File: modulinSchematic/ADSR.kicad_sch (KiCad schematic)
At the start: 0 parts

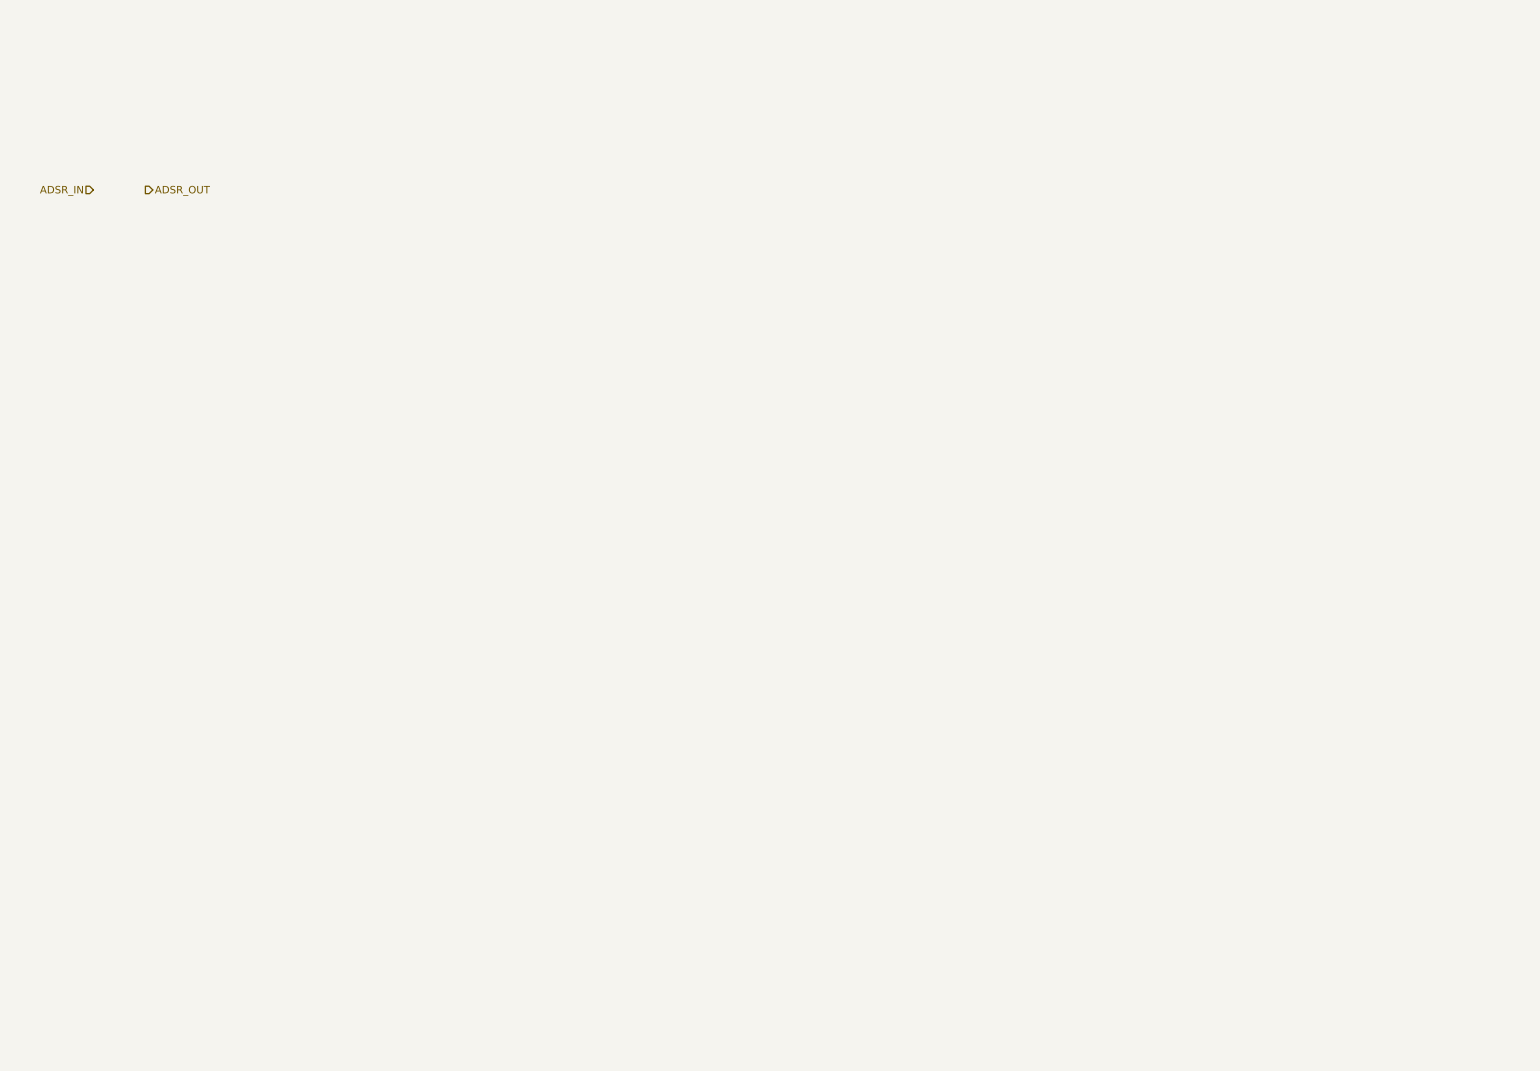
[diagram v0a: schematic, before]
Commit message: Add power schematic
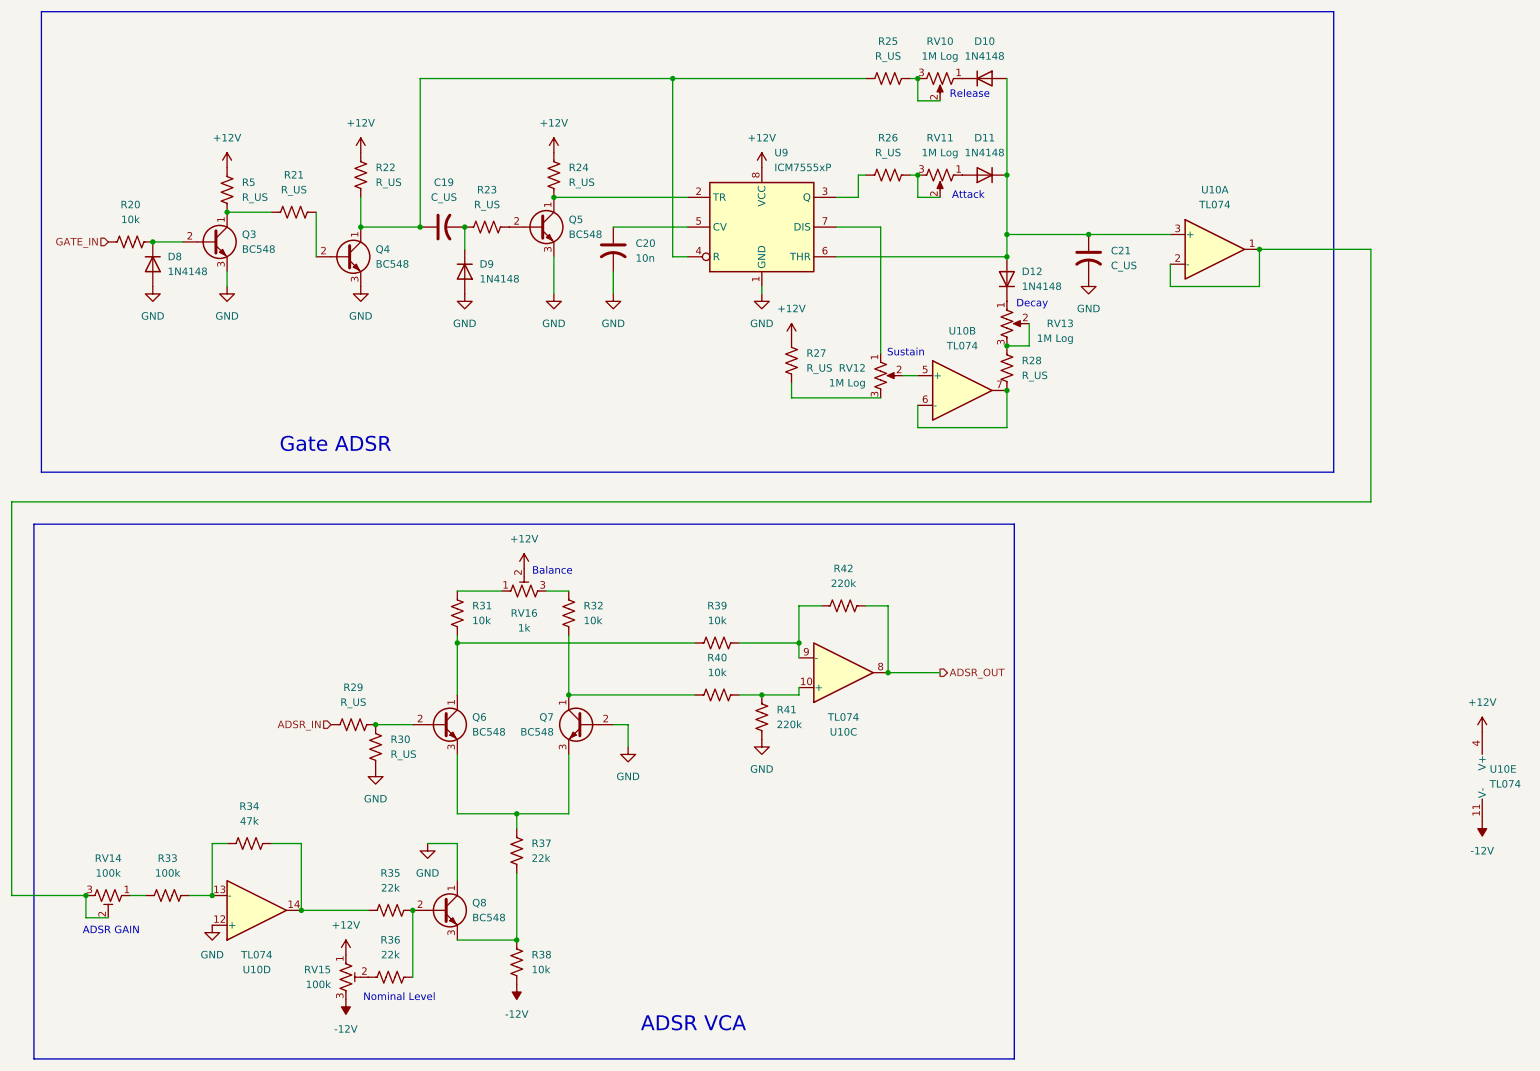
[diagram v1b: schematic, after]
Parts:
- added C19, C21: C_US, Capacitor_THT:CP_Radial_D4.0mm_P2.00mm, symbol Device:C_US
- added C20: 10n, Capacitor_THT:CP_Radial_D4.0mm_P2.00mm, symbol Device:C_US
- added D10, D11, D12, D8, D9: 1N4148, Diode_THT:D_DO-35_SOD27_P7.62mm_Horizontal, symbol Diode:1N4148
- added Q3, Q4, Q5, Q6, Q7, Q8: BC548, Package_TO_SOT_THT:TO-92_Inline, symbol Transistor_BJT:BC548
- added R20, R31, R32, R38, R39, R40: 10k, Resistor_THT:R_Axial_DIN0207_L6.3mm_D2.5mm_P10.16mm_Horizontal, symbol Device:R_US
- added R21, R22, R23, R24, R25, R26, R27, R28, R29, R30, R5: R_US, Resistor_THT:R_Axial_DIN0207_L6.3mm_D2.5mm_P10.16mm_Horizontal, symbol Device:R_US
- added R33: 100k, Resistor_THT:R_Axial_DIN0207_L6.3mm_D2.5mm_P10.16mm_Horizontal, symbol Device:R_US
- added R34: 47k, Resistor_THT:R_Axial_DIN0207_L6.3mm_D2.5mm_P10.16mm_Horizontal, symbol Device:R_US
- added R35, R36, R37: 22k, Resistor_THT:R_Axial_DIN0207_L6.3mm_D2.5mm_P10.16mm_Horizontal, symbol Device:R_US
- added R41, R42: 220k, Resistor_THT:R_Axial_DIN0207_L6.3mm_D2.5mm_P10.16mm_Horizontal, symbol Device:R_US
- added RV10, RV11, RV12, RV13: 1M Log, TerminalBlock:TerminalBlock_MaiXu_MX126-5.0-03P_1x03_P5.00mm, symbol Device:R_Potentiometer_US
- added RV14, RV15: 100k, Potentiometer_THT:Potentiometer_Bourns_3266Y_Vertical, symbol Device:R_Potentiometer_Trim_US
- added RV16: 1k, Potentiometer_THT:Potentiometer_Bourns_3266Y_Vertical, symbol Device:R_Potentiometer_Trim_US
- added U10: TL074, Package_DIP:DIP-14_W7.62mm, symbol Amplifier_Operational:TL074
- added U9: ICM7555xP, Package_DIP:DIP-8_W7.62mm, symbol Timer:ICM7555xP
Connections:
- net ADSR_IN: now also R29.1
- net ADSR_OUT: now also R42.2, U10.8
- new net: Q5.1 (C), R24.2, U9.2 (TR)
- new net: R26.1, U9.3 (Q)
- new net: C19.1, Q4.1 (C), R22.2, R25.1, U9.4 (R)
- new net: C20.1, U9.5 (CV)
- new net: C21.1, D10.2 (A), D11.1 (K), D12.2 (A), U10.3 (+), U9.6 (THR)
- new net: RV12.1, U9.7 (DIS)
- new net: Q7.1 (C), R32.1, R40.2
- new net: R32.2, RV16.3
- new net: R34.2, R35.1, U10.14
- new net: Q8.2 (B), R35.2, R36.2
- new net: R40.1, R41.1, U10.10 (+)
- new net: R27.1, RV12.3
- new net: R36.1, RV15.2
- new net: D12.1 (K), RV13.1
- new net: Q3.1 (C), R21.1, R5.2
- new net: Q4.2 (B), R21.2
- new net: R39.1, R42.1, U10.9 (-)
- new net: D11.2 (A), RV11.1
- new net: Q6.2 (B), R29.2, R30.2
- new net: D10.1 (K), RV10.1
- new net: D8.1 (K), Q3.2 (B), R20.2
- new net: Q6.1 (C), R31.1, R39.2
- new net: R25.2, RV10.2, RV10.3
- new net: C19.2, D9.1 (K), R23.1
- new net: Q6.3 (E), Q7.3 (E), R37.2
- new net: R28.2, RV13.2, RV13.3
- new net: R33.1, RV14.1
- new net: RV14.2, RV14.3, U10.1, U10.2 (-)
- new net: RV12.2, U10.5 (+)
- new net: R31.2, RV16.1
- new net: Q5.2 (B), R23.2
- new net: R33.2, R34.1, U10.13 (-)
- new net: Q8.3 (E), R37.1, R38.2
- new net: R28.1, U10.6 (-), U10.7
- new net: R26.2, RV11.2, RV11.3
- new net +12V: R22.1, R24.1, R27.2, R5.1, RV15.1, RV16.2, U10.4 (V+), U9.8 (VCC)
- new net -12V: R38.1, RV15.3, U10.11 (V-)
- new net GATE_IN: R20.1
- new net GND: C20.2, C21.2, D8.2 (A), D9.2 (A), Q3.3 (E), Q4.3 (E), Q5.3 (E), Q7.2 (B), Q8.1 (C), R30.1, R41.2, U10.12 (+), U9.1 (GND)
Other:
- note added: "ADSR GAIN"
- note added: "ADSR VCA"
- note added: "Attack"
- note added: "Balance"
- note added: "Decay"
- note added: "Gate ADSR"
- note added: "Nominal Level"
- note added: "Release"
- note added: "Sustain"
